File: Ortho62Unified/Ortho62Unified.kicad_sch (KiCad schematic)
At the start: 182 parts, among them J1 AVR-PDI-6, J3 USB_C_Receptacle_USB2.0, SW1 SW_Push, SW10 SW_Push, SW11 SW_Push, SW12 SW_Push, SW13 SW_Push, SW14 SW_Push, SW15 SW_Push, SW16 SW_Push, SW17 SW_Push, SW18 SW_Push, SW19 SW_Push, SW2 SW_Push, SW20 SW_Push, SW21 SW_Push, SW22 SW_Push, SW23 SW_Push, SW24 SW_Push, SW25 SW_Push, SW26 SW_Push, SW27 SW_Push, SW28 SW_Push, SW29 SW_Push, SW3 SW_Push, SW30 SW_Push, SW31 SW_Push, SW32 SW_Push, SW33 SW_Push, SW34 SW_Push, SW35 SW_Push, SW36 SW_Push, SW37 SW_Push, SW38 SW_Push, SW39 SW_Push, SW4 SW_Push, SW40 SW_Push, SW41 SW_Push, SW42 SW_Push, SW43 SW_Push, SW44 SW_Push, SW45 SW_Push, SW46 SW_Push, SW47 SW_Push, SW48 SW_Push, SW49 SW_Push, SW5 SW_Push, SW50 SW_Push, SW51 SW_Push, SW52 SW_Push, SW53 SW_Push, SW54 SW_Push, SW55 SW_Push, SW56 SW_Push, SW57 SW_Push, SW58 SW_Push, SW59 SW_Push, SW6 SW_Push, SW60 SW_Push, SW61 SW_Push, SW62 SW_Push, SW63 SW_Push, SW64 SW_Push, SW65 SW_Push, SW66 SW_Push, SW67 SW_Push, SW68 SW_Push, SW69 SW_Push, SW7 SW_Push, SW70 SW_Push, SW71 SW_Push, SW72 SW_Push, SW73 SW_Push, SW74 SW_Push, SW75 SW_Push, SW76 SW_Push, SW77 SW_Push, SW78 SW_Push, SW79 SW_Push, SW8 SW_Push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

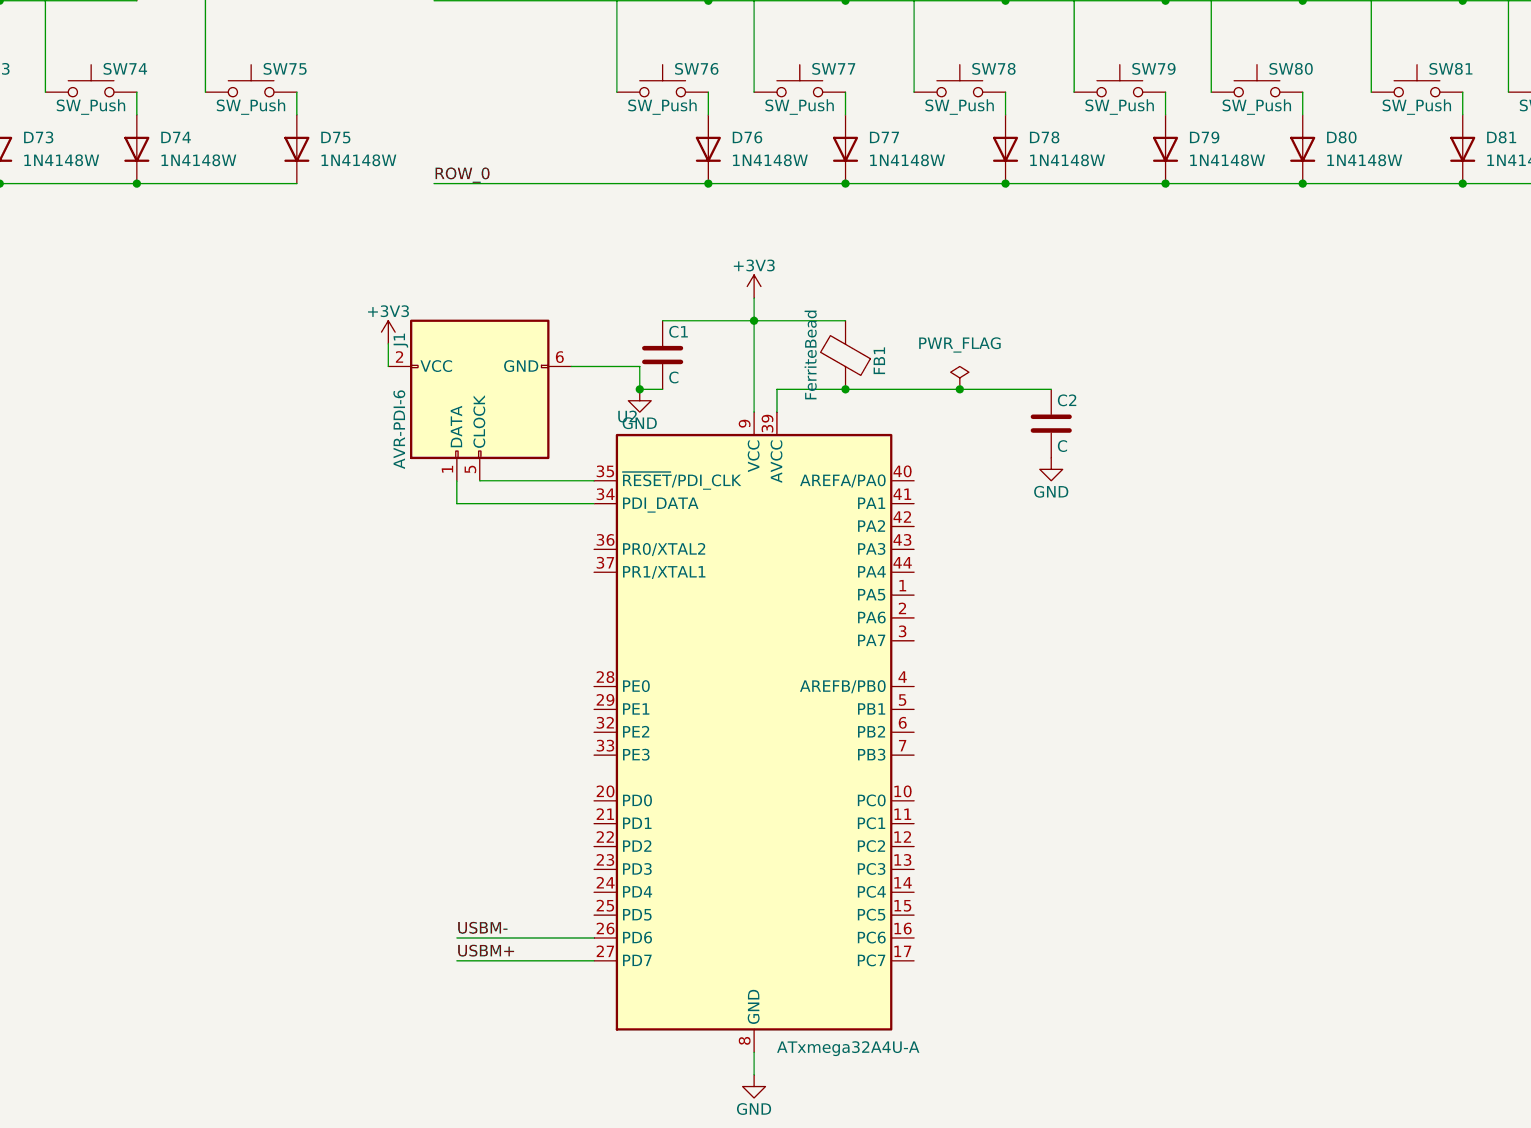
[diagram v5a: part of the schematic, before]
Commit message: Route rows and colums of keyboard matrix to 1.27mm headers.
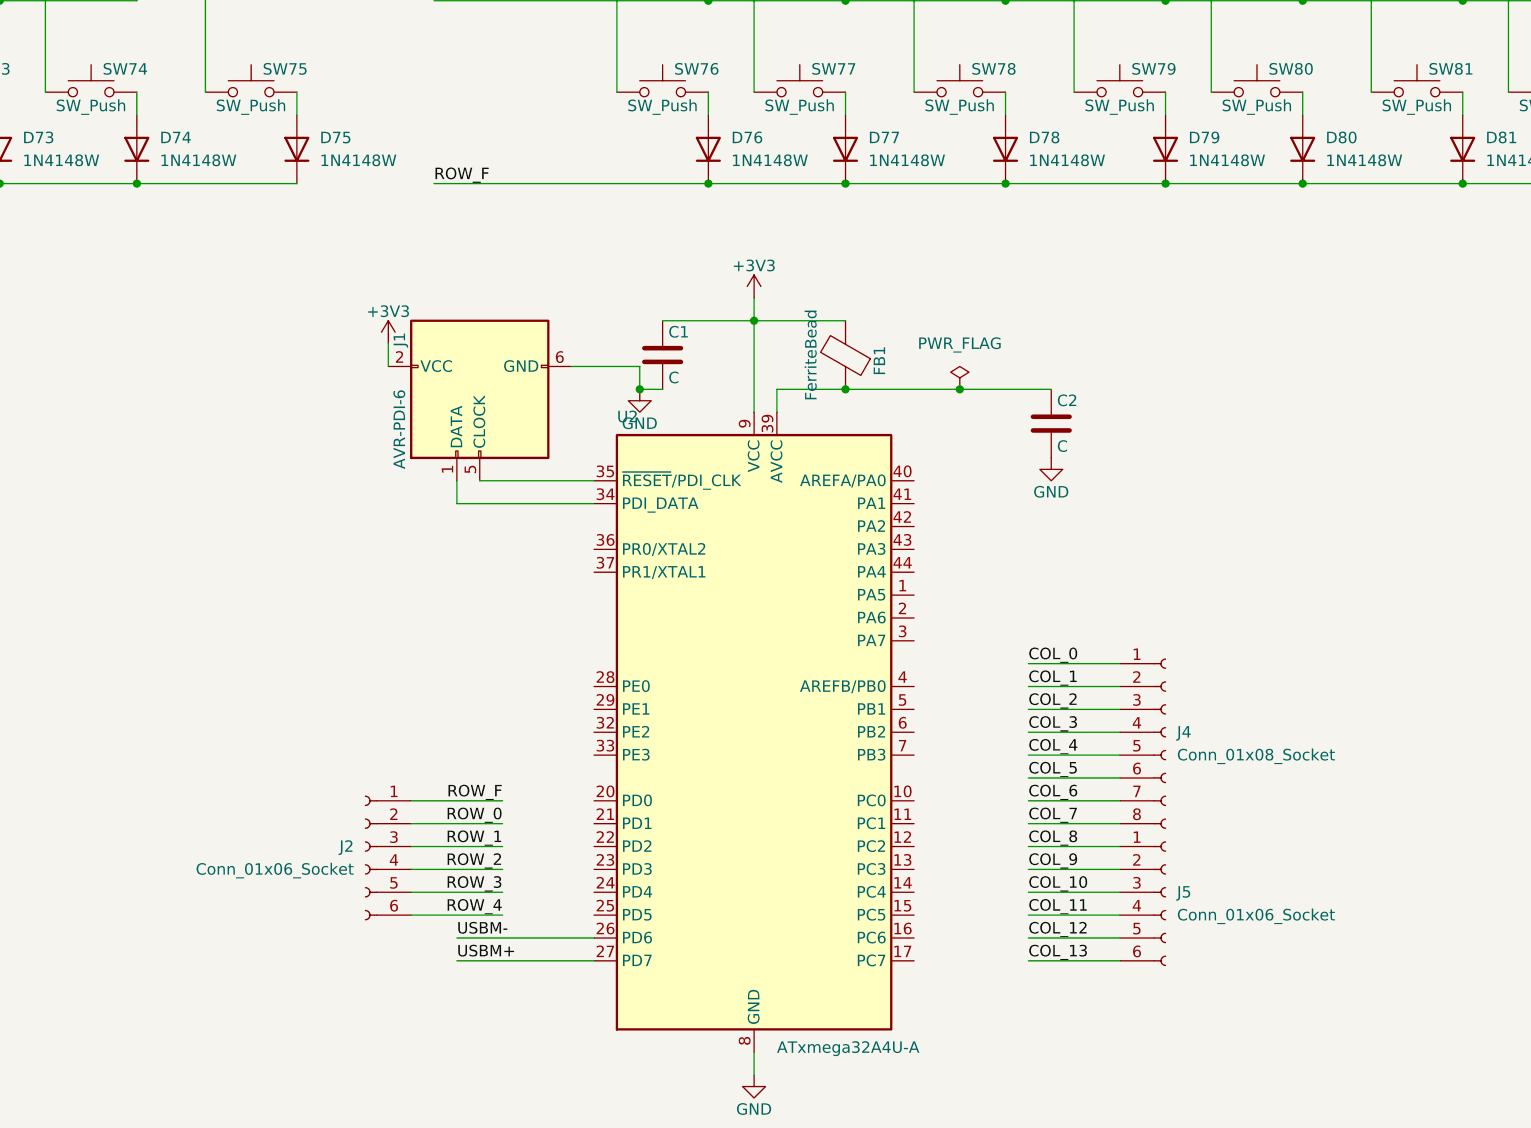
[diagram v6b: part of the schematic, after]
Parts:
- added J2, J5: Conn_01x06_Socket, Connector_PinHeader_1.27mm:PinHeader_1x06_P1.27mm_Vertical, symbol Connector:Conn_01x06_Socket
- added J4: Conn_01x08_Socket, Connector_PinHeader_1.27mm:PinHeader_1x08_P1.27mm_Vertical, symbol Connector:Conn_01x08_Socket
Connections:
- net COL_0: now also J4.1 (Pin_1)
- net COL_1: now also J4.2 (Pin_2)
- net COL_10: now also J5.3 (Pin_3)
- net COL_11: now also J5.4 (Pin_4)
- net COL_12: now also J5.5 (Pin_5)
- net COL_13: now also J5.6 (Pin_6)
- net COL_2: now also J4.3 (Pin_3)
- net COL_3: now also J4.4 (Pin_4)
- net COL_4: now also J4.5 (Pin_5)
- net COL_5: now also J4.6 (Pin_6)
- net COL_6: now also J4.7 (Pin_7)
- net COL_7: now also J4.8 (Pin_8)
- net COL_8: now also J5.1 (Pin_1)
- net COL_9: now also J5.2 (Pin_2)
- net ROW_0: now also J2.2 (Pin_2); no longer D76.1 (K), D77.1 (K), D78.1 (K), D79.1 (K), D80.1 (K), D81.1 (K), D82.1 (K)
- net ROW_1: now also J2.3 (Pin_3)
- net ROW_2: now also J2.4 (Pin_4)
- net ROW_3: now also J2.5 (Pin_5)
- net ROW_4: now also J2.6 (Pin_6)
- net ROW_F: now also D76.1 (K), D77.1 (K), D78.1 (K), D79.1 (K), D80.1 (K), D81.1 (K), D82.1 (K), J2.1 (Pin_1)

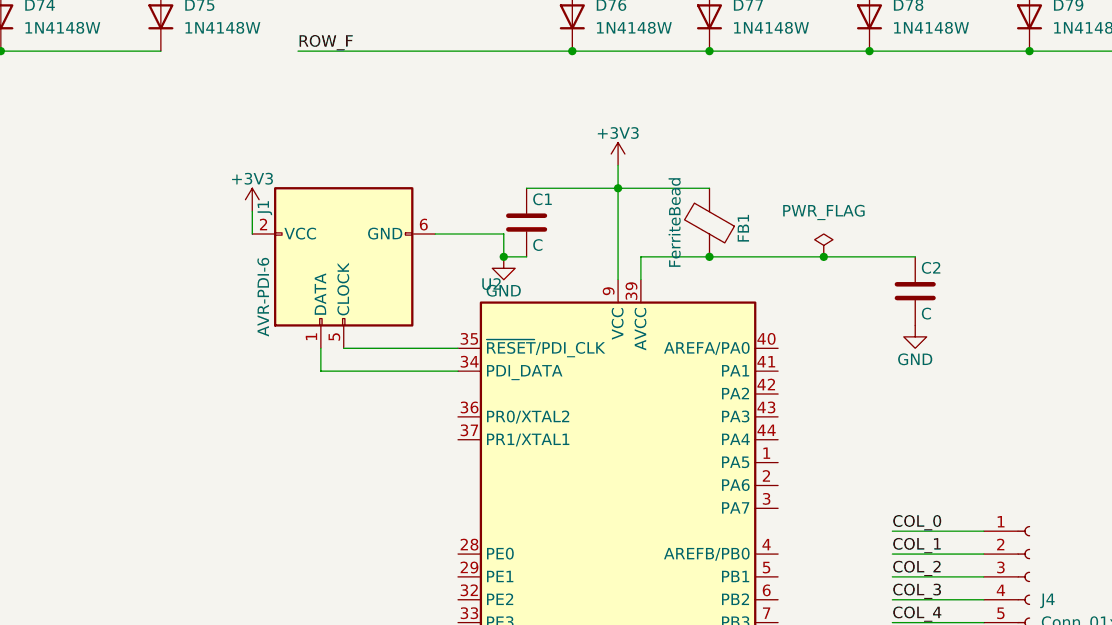
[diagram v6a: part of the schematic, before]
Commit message: Consolitate and place Xmega and USB components.
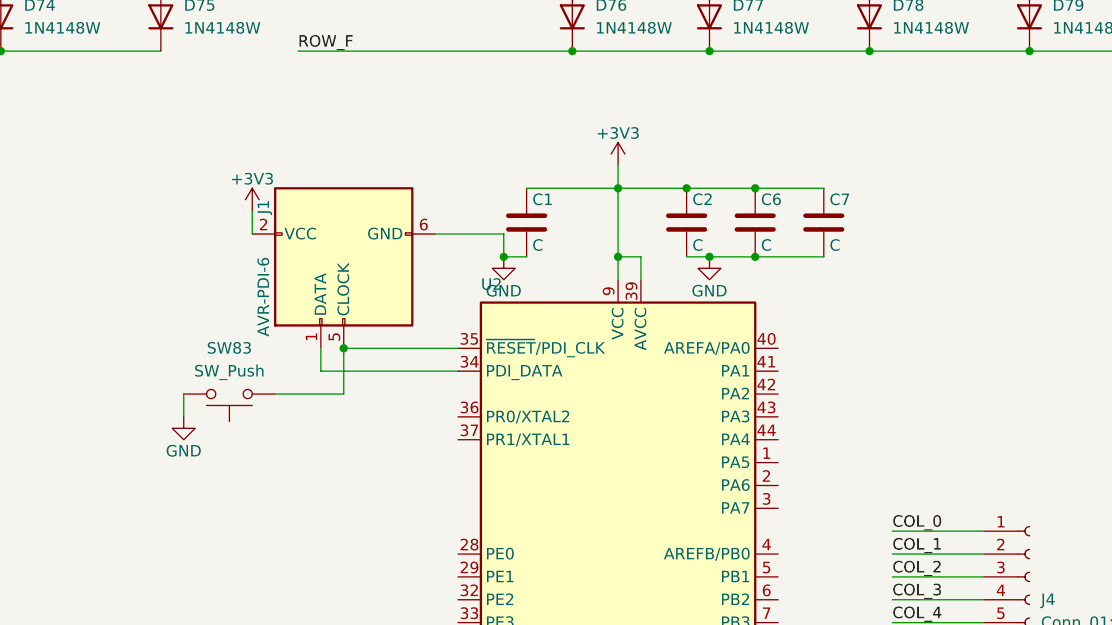
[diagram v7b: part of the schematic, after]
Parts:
- removed FB1: FerriteBead, Inductor_SMD:L_0603_1608Metric_Pad1.05x0.95mm_HandSolder, symbol Device:FerriteBead
- added C6, C7: C, Capacitor_SMD:C_0603_1608Metric_Pad1.08x0.95mm_HandSolder, symbol Device:C
- added SW83: SW_Push, Button_Switch_SMD:SW_Tactile_SPST_NO_Straight_CK_PTS636Sx25SMTRLFS, symbol Switch:SW_Push
- J1: footprint Connector_PinHeader_2.54mm:PinHeader_2x03_P2.54mm_Horizontal -> Connector_PinSocket_2.54mm:PinSocket_1x06_P2.54mm_Vertical
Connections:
- net +3V3: now also C2.1, U2.39 (AVCC), C6.1, C7.1
- net GND: now also C6.2, C7.2, SW83.2
- net at J1.5 (CLOCK), U2.35 (~{RESET}/PDI_CLK): now also SW83.1

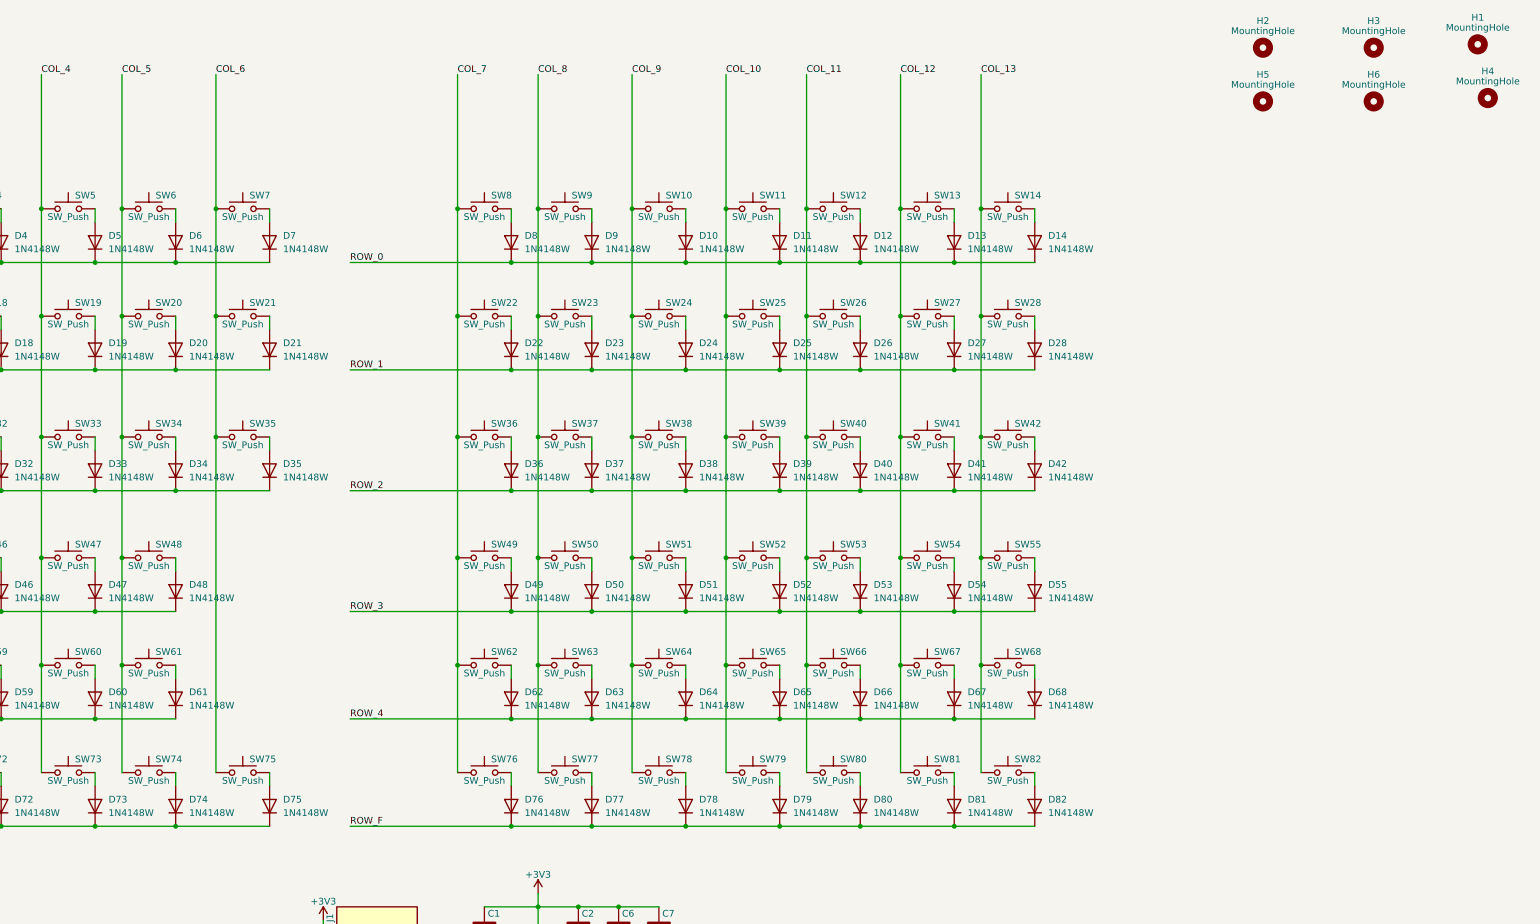
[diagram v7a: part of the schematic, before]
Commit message: Remove F6,F7,F8 keys to create space for controller.
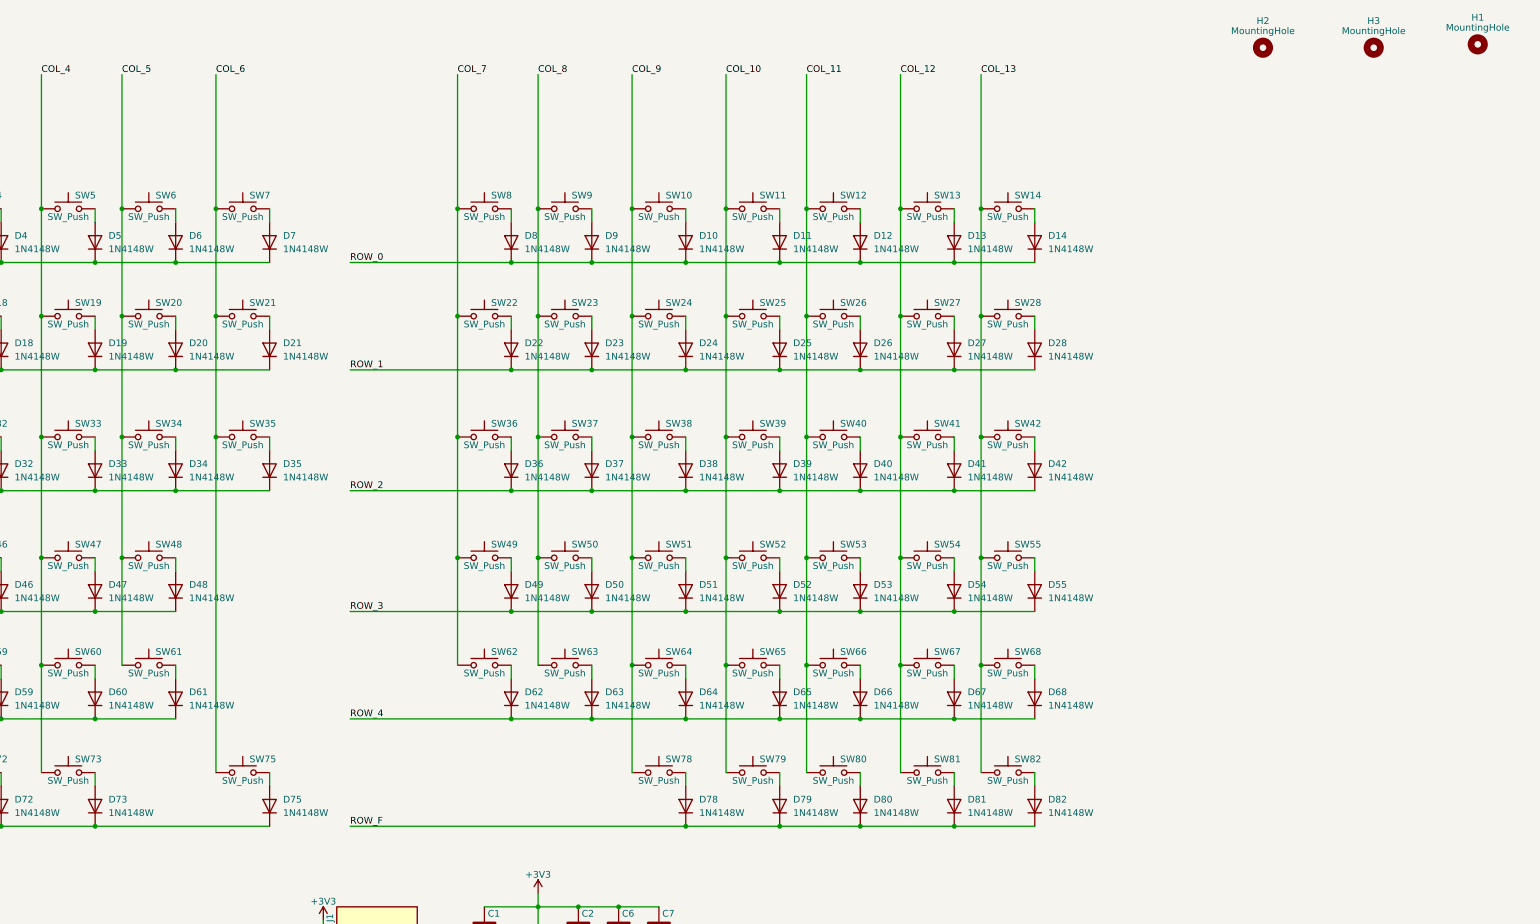
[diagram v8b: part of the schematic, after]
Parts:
- removed D74, D76, D77: 1N4148W, Diode_SMD:D_SOD-123, symbol Diode:1N4148W
- removed H4, H5, H6: MountingHole, MountingHole:MountingHole_3.2mm_M3, symbol Mechanical:MountingHole
- removed SW74, SW76, SW77: SW_Push, Switch_Keyboard_Kailh:SW_Kailh_Choc_V1V2_1.00u, symbol Switch:SW_Push
- J1: footprint Connector_PinSocket_2.54mm:PinSocket_1x06_P2.54mm_Vertical -> Connector_PinHeader_2.54mm:PinHeader_2x03_P2.54mm_Horizontal
